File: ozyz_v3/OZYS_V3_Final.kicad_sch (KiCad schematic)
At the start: 39 parts, among them CN1 532610571, Q3 2N7002, U1 ISO1044BD, U2 STM32G474CETx, U3 MKDV32GCL-STP, U5 RH-5015, U6 RH-5015, U7 RH-5015, U8 RH-5015, U9 RH-5015, X1 X322516MLB4SI, X2 MC-306 32.768kHz 6.0pF 20ppm

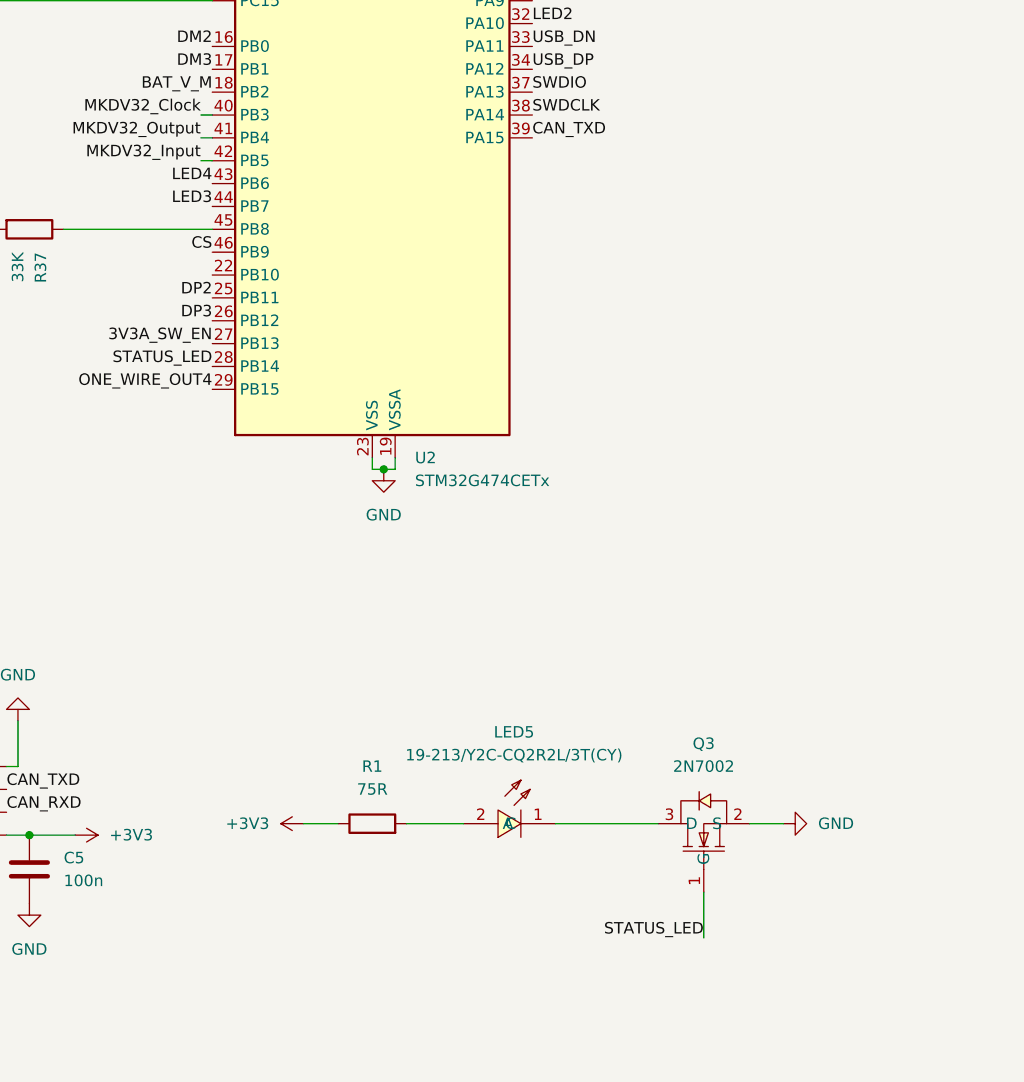
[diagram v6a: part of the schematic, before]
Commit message: Got rid of LED Fet
- restructuring
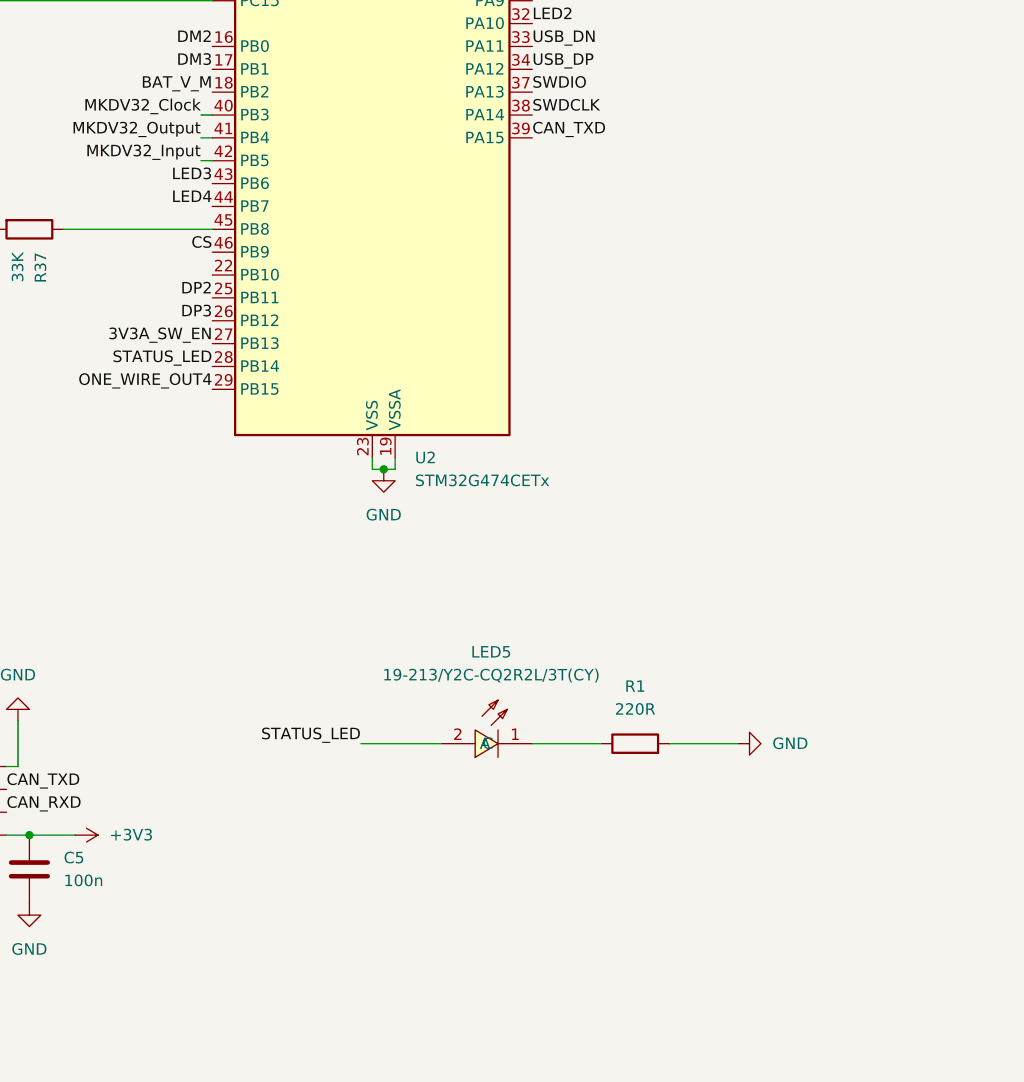
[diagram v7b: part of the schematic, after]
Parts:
- removed Q3: 2N7002, Rocketry_Easyeda:SOT-23-3_L2.9-W1.3-P1.90-LS2.4-BR, symbol Rocketry_Easyeda:2N7002
- R1: value 75R -> 220R
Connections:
- net +3V3: no longer R1.1
- net GND: now also R1.2
- net LED3: now also U2.43 (PB6); no longer U2.44 (PB7)
- net LED4: now also U2.44 (PB7); no longer U2.43 (PB6)
- net STATUS_LED: now also LED5.2 (A)
- net at LED5.1 (C): now also R1.1

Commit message: final touches
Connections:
- net ONE_WIRE_OUT1: no longer U7.1
- net ONE_WIRE_OUT3: now also U7.1
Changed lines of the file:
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@@
 		)
 	)
-	(label "ONE_WIRE_OUT1"
+	(label "ONE_WIRE_OUT3"
 		(at 226.06 80.01 0)
 		(effects
